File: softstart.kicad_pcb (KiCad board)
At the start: 2 copper layers, 39.4 x 39.4 mm, 21 parts, among them J1 Conn_01x02, Q1 IRF100B201, Q2 IRF100B201, U1 L78L15_TO92, U2 LM393

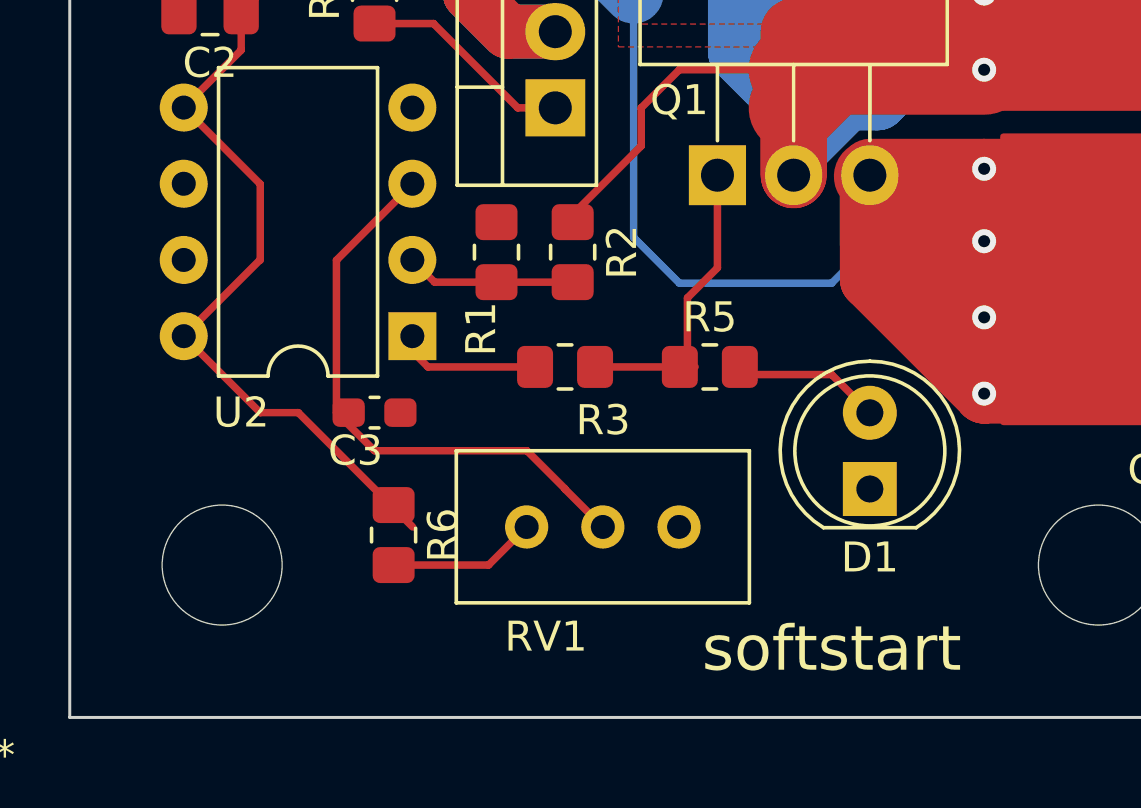
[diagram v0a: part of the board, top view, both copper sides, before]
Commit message: fix comp output
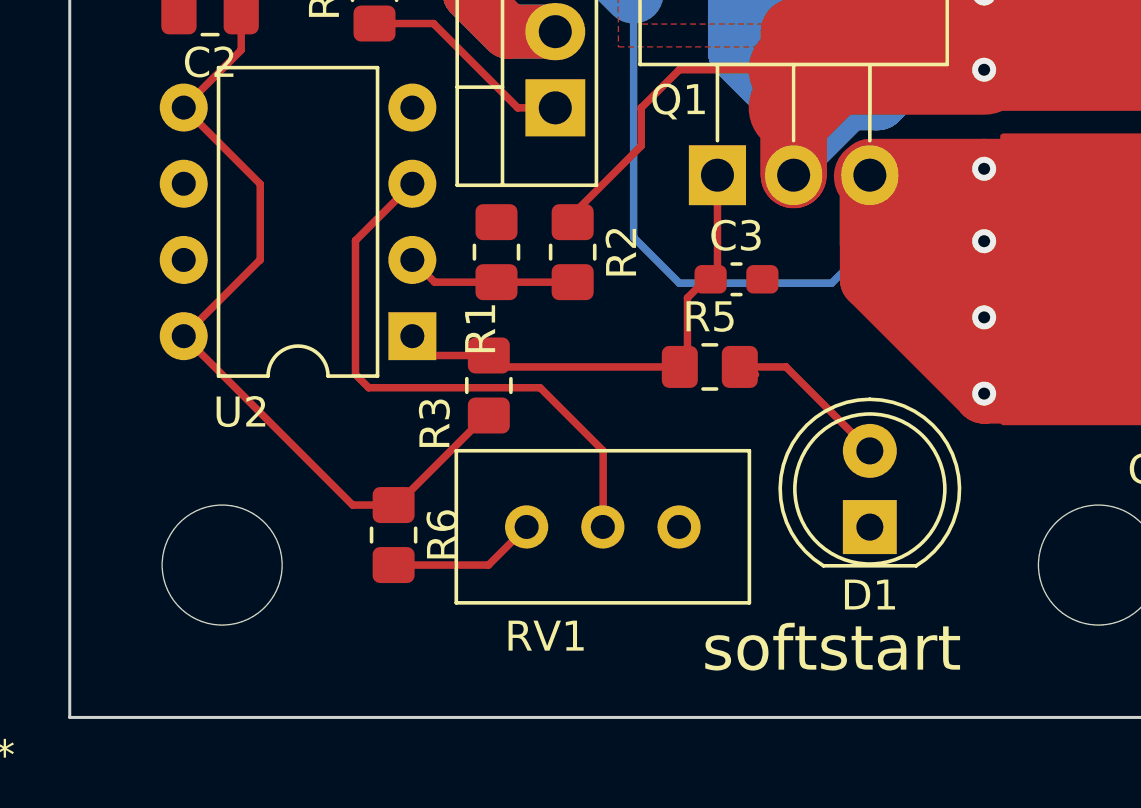
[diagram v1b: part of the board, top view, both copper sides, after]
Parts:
- C3: value 2.2n -> 100n
- R3, R4: value 330 -> 1k
- moved C3 12.9 mm to (174.6, 73.0)
- moved R3 2.61 mm to (166.4, 76.6), turned to -90 degrees
- moved D1 1.27 mm to (179.1, 81.3)
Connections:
- C3 pad 1: Net-(C3-Pad1) -> Net-(Q1-Pad1)
- R3 pad 1: Net-(R3-Pad1) -> Net-(Q1-Pad1)
- R3 pad 2: Net-(Q1-Pad1) -> +15V
- RV1 pad 2: Net-(C3-Pad1) -> Net-(RV1-Pad2)
- U2 pad 1: Net-(R3-Pad1) -> Net-(Q1-Pad1)
- U2 pad 3: Net-(C3-Pad1) -> Net-(RV1-Pad2)
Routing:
- net Net-(C3-Pad1): track 19.2 -> 0.00 mm
- net Net-(RV1-Pad2): track 0.00 -> 19.0 mm
- net Net-(Q1-Pad1): track 10.1 -> 16.7 mm
- net Net-(R3-Pad1): track 4.81 -> 0.00 mm
- net +15V: track 30.1 -> 34.3 mm
- net Net-(D1-Pad2): track 4.71 -> 5.87 mm
